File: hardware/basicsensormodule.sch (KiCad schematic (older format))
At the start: 6 parts, among them J1 Conn_01x04

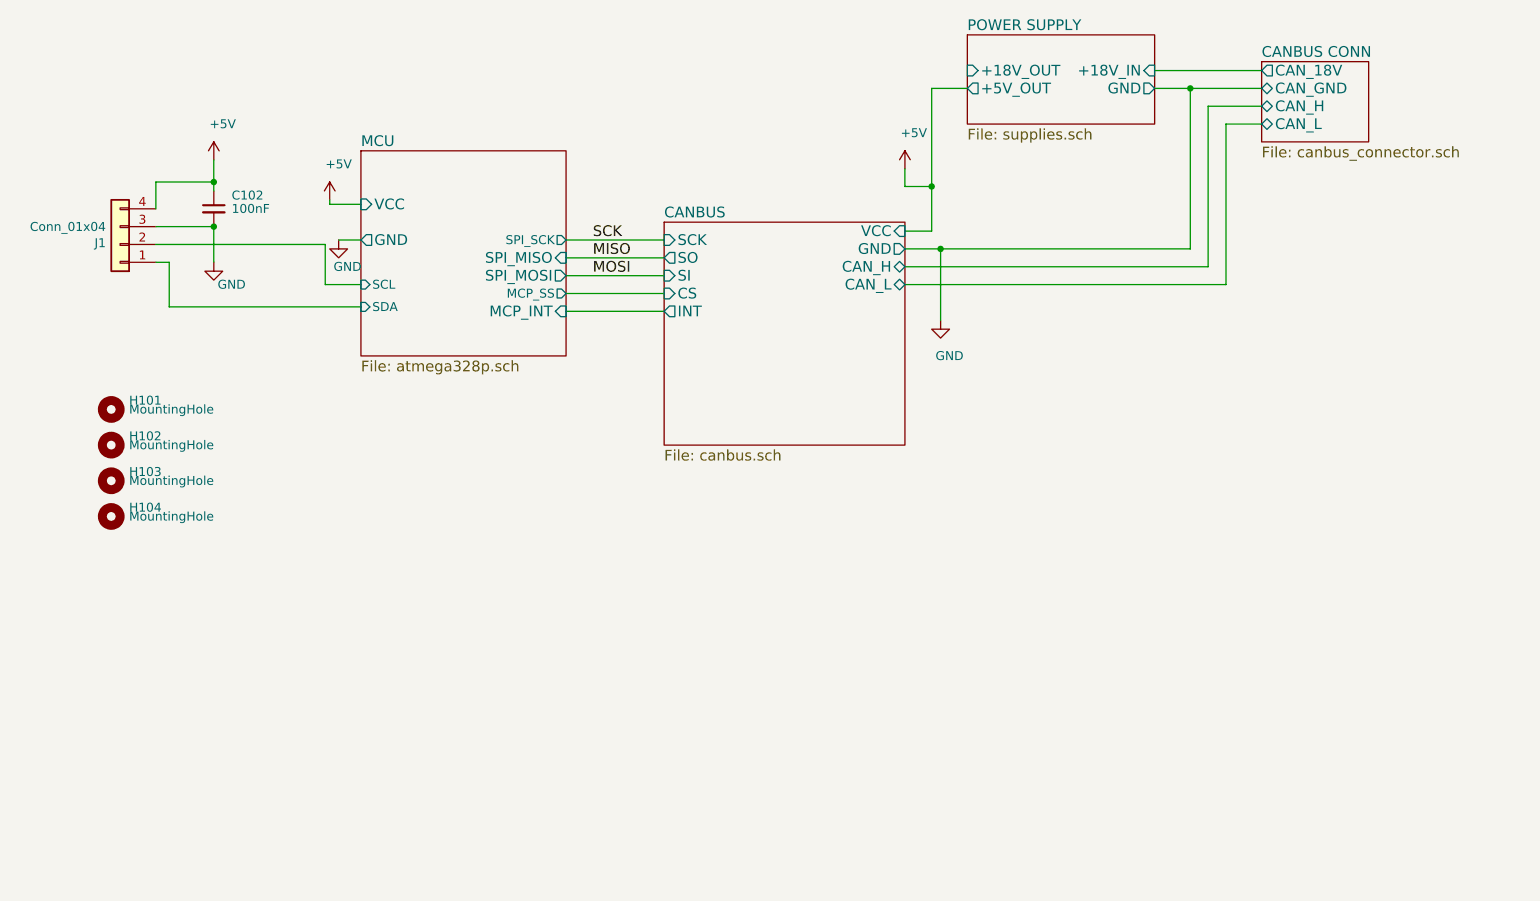
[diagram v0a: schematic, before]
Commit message: Layout MT19 criado para o Taquímetro do barco.
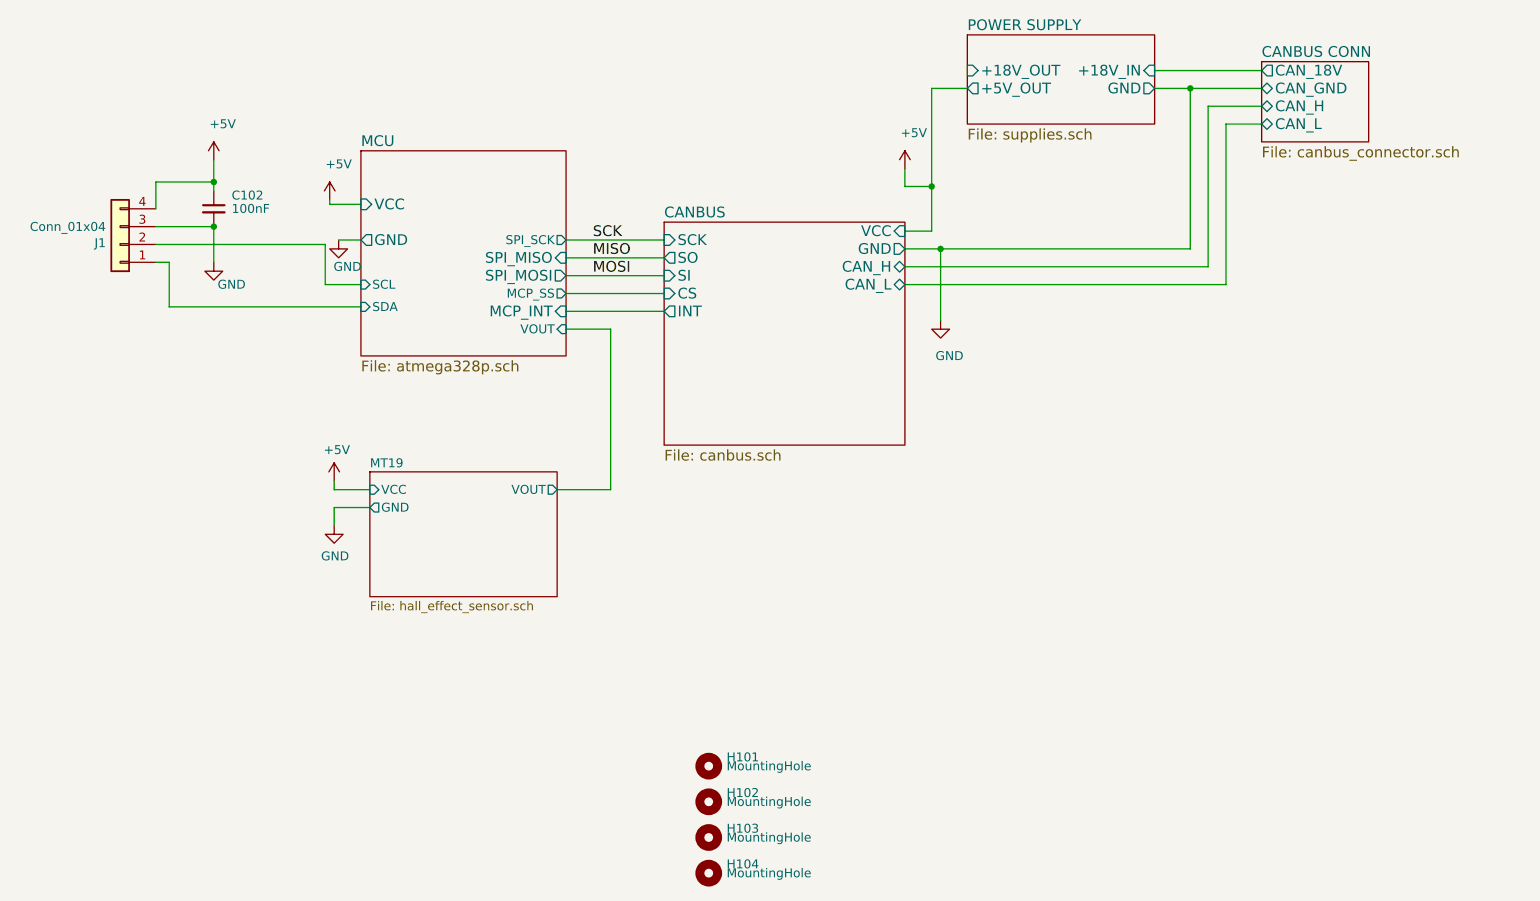
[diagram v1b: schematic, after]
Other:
- moved on the sheet: H101, H102, H103, H104
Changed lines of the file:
@@
 EESchema Schematic File Version 4
 LIBS:basicsensormodule-cache
-EELAYER 26 0
+EELAYER 29 0
 EELAYER END
 $Descr A4 11693 8268
 encoding utf-8
-Sheet 1 5
+Sheet 1 6
 Title ""
 Date ""
@@
 F9 "SCL" I L 4350 4350 50
 F10 "SDA" I L 4350 4475 50
+F11 "VOUT" I R 5500 4600 50
 $EndSheet
 $Sheet
@@
 L basicsensormodule-rescue:MountingHole-Mechanical H104
 U 1 1 5BE9AF15
-P 2950 5650
-F 0 "H104" H 3050 5700 50  0000 L CNN
-F 1 "MountingHole" H 3050 5650 50  0000 L CNN
-F 2 "MountingHole:MountingHole_3.2mm_M3" H 2950 5650 50  0001 C CNN
-F 3 "~" H 2950 5650 50  0001 C CNN
-	1    2950 5650
+P 6300 7650
+F 0 "H104" H 6400 7700 50  0000 L CNN
+F 1 "MountingHole" H 6400 7650 50  0000 L CNN
+F 2 "MountingHole:MountingHole_3.2mm_M3" H 6300 7650 50  0001 C CNN
+F 3 "~" H 6300 7650 50  0001 C CNN
+	1    6300 7650
 	1    0    0    -1
 $EndComp
@@
 L basicsensormodule-rescue:MountingHole-Mechanical H103
 U 1 1 5BE9BC53
-P 2950 5450
-F 0 "H103" H 3050 5500 50  0000 L CNN
-F 1 "MountingHole" H 3050 5450 50  0000 L CNN
-F 2 "MountingHole:MountingHole_3.2mm_M3" H 2950 5450 50  0001 C CNN
-F 3 "~" H 2950 5450 50  0001 C CNN
-	1    2950 5450
+P 6300 7450
+F 0 "H103" H 6400 7500 50  0000 L CNN
+F 1 "MountingHole" H 6400 7450 50  0000 L CNN
+F 2 "MountingHole:MountingHole_3.2mm_M3" H 6300 7450 50  0001 C CNN
+F 3 "~" H 6300 7450 50  0001 C CNN
+	1    6300 7450
 	1    0    0    -1
 $EndComp
@@
 L basicsensormodule-rescue:MountingHole-Mechanical H102
 U 1 1 5BE9BC79
-P 2950 5250
-F 0 "H102" H 3050 5300 50  0000 L CNN
-F 1 "MountingHole" H 3050 5250 50  0000 L CNN
-F 2 "MountingHole:MountingHole_3.2mm_M3" H 2950 5250 50  0001 C CNN
-F 3 "~" H 2950 5250 50  0001 C CNN
-	1    2950 5250
+P 6300 7250
+F 0 "H102" H 6400 7300 50  0000 L CNN
+F 1 "MountingHole" H 6400 7250 50  0000 L CNN
+F 2 "MountingHole:MountingHole_3.2mm_M3" H 6300 7250 50  0001 C CNN
+F 3 "~" H 6300 7250 50  0001 C CNN
+	1    6300 7250
 	1    0    0    -1
 $EndComp
@@
 L basicsensormodule-rescue:MountingHole-Mechanical H101
 U 1 1 5BE9BC9F
-P 2950 5050
-F 0 "H101" H 3050 5100 50  0000 L CNN
-F 1 "MountingHole" H 3050 5050 50  0000 L CNN
-F 2 "MountingHole:MountingHole_3.2mm_M3" H 2950 5050 50  0001 C CNN
-F 3 "~" H 2950 5050 50  0001 C CNN
-	1    2950 5050
+P 6300 7050
+F 0 "H101" H 6400 7100 50  0000 L CNN
+F 1 "MountingHole" H 6400 7050 50  0000 L CNN
+F 2 "MountingHole:MountingHole_3.2mm_M3" H 6300 7050 50  0001 C CNN
+F 3 "~" H 6300 7050 50  0001 C CNN
+	1    6300 7050
 	1    0    0    -1
 $EndComp
@@
 Wire Wire Line
 	4175 3900 4175 3875
+$Sheet
+S 4400 5400 1050 700
+U 5CD559BA
+F0 "MT19" 50
+F1 "hall_effect_sensor.sch" 50
+F2 "VCC" I L 4400 5500 50
+F3 "GND" O L 4400 5600 50
+F4 "VOUT" O R 5450 5500 50
+$EndSheet
+$Comp
+L power:GND #PWR0108
+U 1 1 5CD759B4
+P 4200 5700
+F 0 "#PWR0108" H 4200 5450 50  0001 C CNN
+F 1 "GND" H 4205 5527 50  0000 C CNN
+F 2 "" H 4200 5700 50  0001 C CNN
+F 3 "" H 4200 5700 50  0001 C CNN
+	1    4200 5700
+	1    0    0    -1
+$EndComp
+Wire Wire Line
+	4400 5600 4200 5600
+Wire Wire Line
+	4200 5600 4200 5700
+$Comp
+L power:+5V #PWR0109
+U 1 1 5CD76A38
+P 4200 5450
+F 0 "#PWR0109" H 4200 5300 50  0001 C CNN
+F 1 "+5V" H 4215 5623 50  0000 C CNN
+F 2 "" H 4200 5450 50  0001 C CNN
+F 3 "" H 4200 5450 50  0001 C CNN
+	1    4200 5450
+	1    0    0    -1
+$EndComp
+Wire Wire Line
+	4400 5500 4200 5500
+Wire Wire Line
+	4200 5500 4200 5450
+Wire Wire Line
+	5500 4600 5750 4600
+Wire Wire Line
+	5750 4600 5750 5500
+Wire Wire Line
+	5750 5500 5450 5500
 $EndSCHEMATC
